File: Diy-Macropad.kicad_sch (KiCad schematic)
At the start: 28 parts, among them J1 Conn_01x04, SW1 RotaryEncoder_Switch, U1 MCU_Seeed_XIAO_RP2040

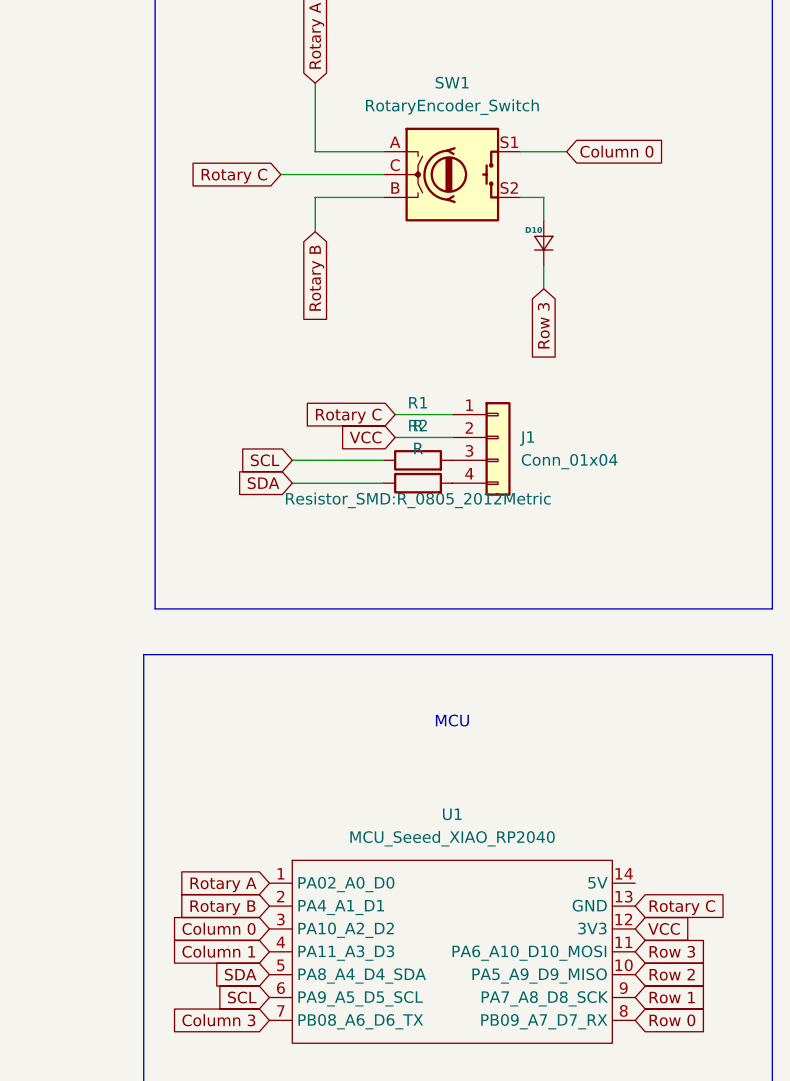
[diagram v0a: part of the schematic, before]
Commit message: added copper ground
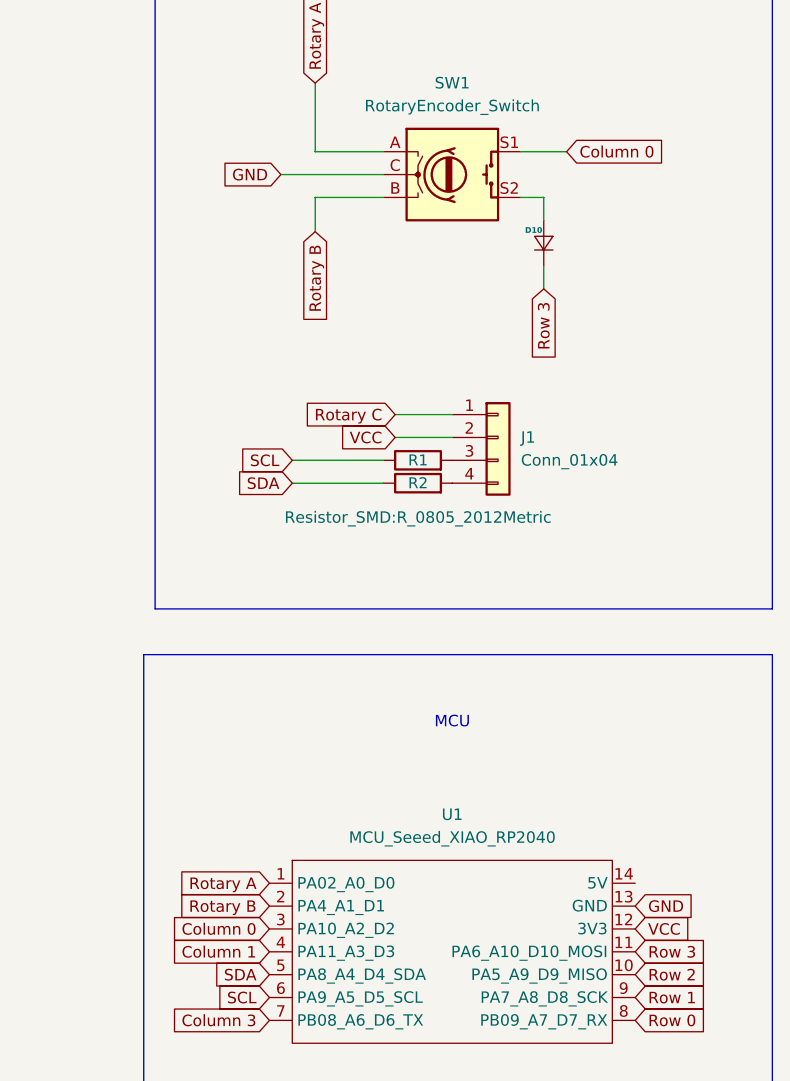
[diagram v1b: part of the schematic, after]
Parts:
- H1, H2, H3, H4: footprint MountingHole:MountingHole_2.2mm_M2 -> MountingHole:MountingHole_2.2mm_M2_DIN965_Pad
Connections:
- net Rotary C: no longer SW1.C, U1.13 (GND)
- new net GND: SW1.C, U1.13 (GND)
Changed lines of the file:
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@@
 		)
 	)
-	(global_label "Rotary C"
+	(global_label "GND"
 		(shape input)
 		(at 189.23 50.8 180)
@@
 		)
 		(property "Intersheetrefs" "${INTERSHEET_REFS}"
-			(at 177.9597 50.8 0)
+			(at 182.3743 50.8 0)
 			(effects
 				(font
@@
 		)
 	)
-	(global_label "Rotary C"
+	(global_label "GND"
 		(shape input)
 		(at 228.6 132.08 0)
@@
 		)
 		(property "Intersheetrefs" "${INTERSHEET_REFS}"
-			(at 239.8703 132.08 0)
+			(at 235.4557 132.08 0)
 			(effects
 				(font
@@
 		(on_board yes)
 		(dnp no)
-		(fields_autoplaced yes)
 		(property "Reference" "R2"
-			(at 204.47 78.74 90)
-			(effects
-				(font
-					(size 1.27 1.27)
+			(at 204.47 85.09 90)
+			(effects
+				(font
+					(size 1.2192 1.2192)
 				)
 			)
@@
 					(size 1.27 1.27)
 				)
+				(hide yes)
 			)
 		)
 		(property "Footprint" "Resistor_SMD:R_0805_2012Metric"
-			(at 204.47 86.868 90)
+			(at 204.47 88.9 90)
 			(effects
 				(font
@@
 		(on_board yes)
 		(dnp no)
-		(fields_autoplaced yes)
 		(property "Reference" "R1"
-			(at 204.47 76.2 90)
-			(effects
-				(font
-					(size 1.27 1.27)
+			(at 204.47 82.55 90)
+			(effects
+				(font
+					(size 1.2192 1.2192)
 				)
 			)
@@
 					(size 1.27 1.27)
 				)
+				(hide yes)
 			)
 		)
@@
 			)
 		)
-		(property "Footprint" "MountingHole:MountingHole_2.2mm_M2"
+		(property "Footprint" "MountingHole:MountingHole_2.2mm_M2_DIN965_Pad"
 			(at 67.31 153.67 0)
 			(effects
@@
 			)
 		)
-		(property "Footprint" "MountingHole:MountingHole_2.2mm_M2"
+		(property "Footprint" "MountingHole:MountingHole_2.2mm_M2_DIN965_Pad"
 			(at 54.61 153.67 0)
 			(effects
@@
 			)
 		)
-		(property "Footprint" "MountingHole:MountingHole_2.2mm_M2"
+		(property "Footprint" "MountingHole:MountingHole_2.2mm_M2_DIN965_Pad"
 			(at 49.53 153.67 0)
 			(effects
@@
 			)
 		)
-		(property "Footprint" "MountingHole:MountingHole_2.2mm_M2"
+		(property "Footprint" "MountingHole:MountingHole_2.2mm_M2_DIN965_Pad"
 			(at 60.96 153.67 0)
 			(effects
